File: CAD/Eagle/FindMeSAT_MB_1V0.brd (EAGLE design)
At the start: 99 x 49.2 mm, 127 parts, among them IC1111 LM2831YMF, J291 MCX-J-P-X-RA-SM1, J685 SMA_CON, J701 MOLEX_105017-0001, J801 MICROSIM-8P_SDCARD-8P_MOLEX-1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, J901 JST_S3B-XH-A, Q101 ABS07, Q651 ABM3B-16MHZ-10-R50-1-U, U1001 CFPT-141, U101 ATXMEGA256A3BU-AU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

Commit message: Eagle - minor changes done
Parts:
- moved R701 0.64 mm to (94.2, 32.3)
- moved R721 0.64 mm to (90.3, 22.9)
- moved C701 0.63 mm to (91.3, 32.9)
- moved R724 0.63 mm to (91.3, 29.8)
- moved R725 0.63 mm to (90.8, 29.8)
- moved J701 0.51 mm to (98.6, 27.9)
- moved J801 0.25 mm to (26.8, 8.89)
- moved R141 0.18 mm to (71.0, 4.95)
- moved R142 0.13 mm to (71.0, 3.68)
- renumbered IC1111 to U1111
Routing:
- net +3V3: track 58.0 -> 63.1 mm, vias 15 -> 16
- net GND: track 214.5 -> 216.0 mm
- net +5V: track 130.4 -> 129.0 mm
- net J_VUSB: track 7.64 -> 8.29 mm
- net USB_ID: track 38.7 -> 38.0 mm
- net GPS_1PPS: track 52.3 -> 52.8 mm
- net J_D-: track 9.04 -> 8.53 mm
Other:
- board text added: "+"
- board text added: "Bluetooth-Antenna"
- board text added: "GND"
- board text added: "GPS"
- board text added: "GSM-Antenna"
- board text added: "LCD"
- board text added: "LiPo"
- board text added: "PDI"
- board text added: "USB"
- board text added: "VHF"

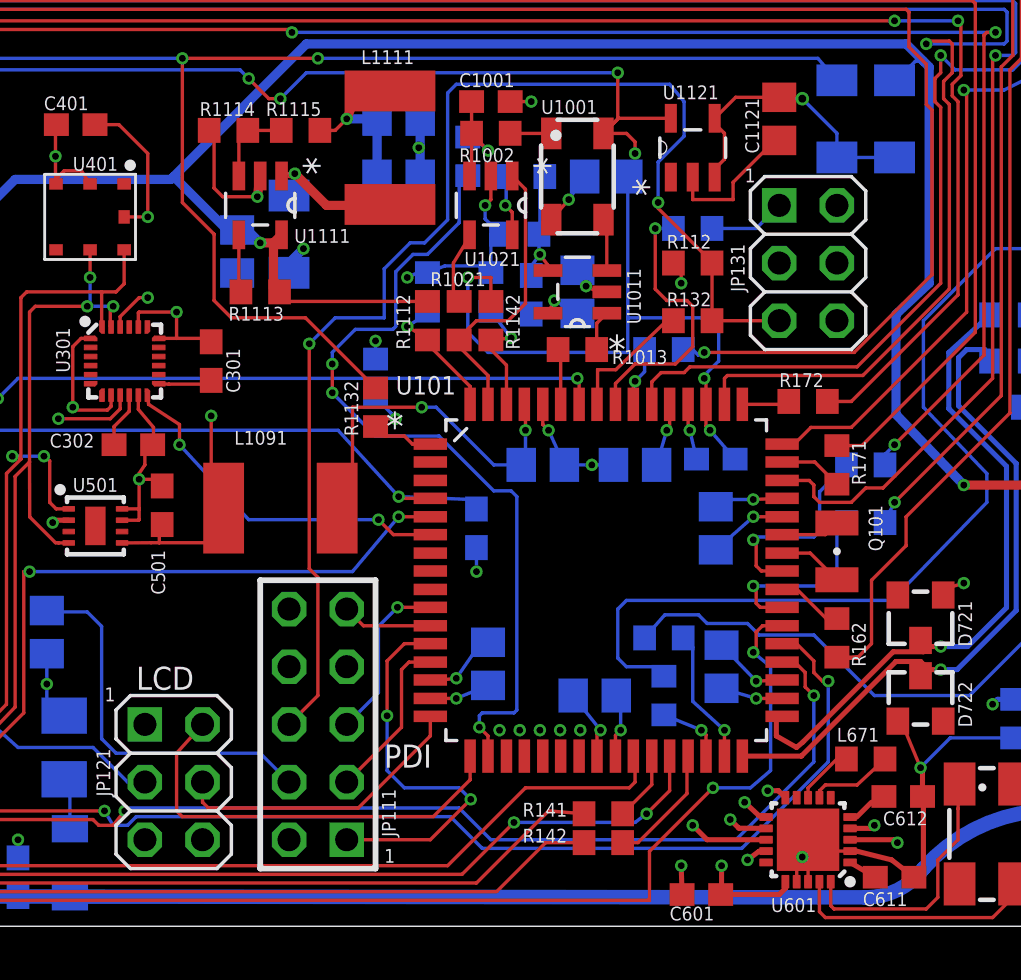
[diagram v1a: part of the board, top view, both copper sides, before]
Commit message: Eagle - values corrected and placed
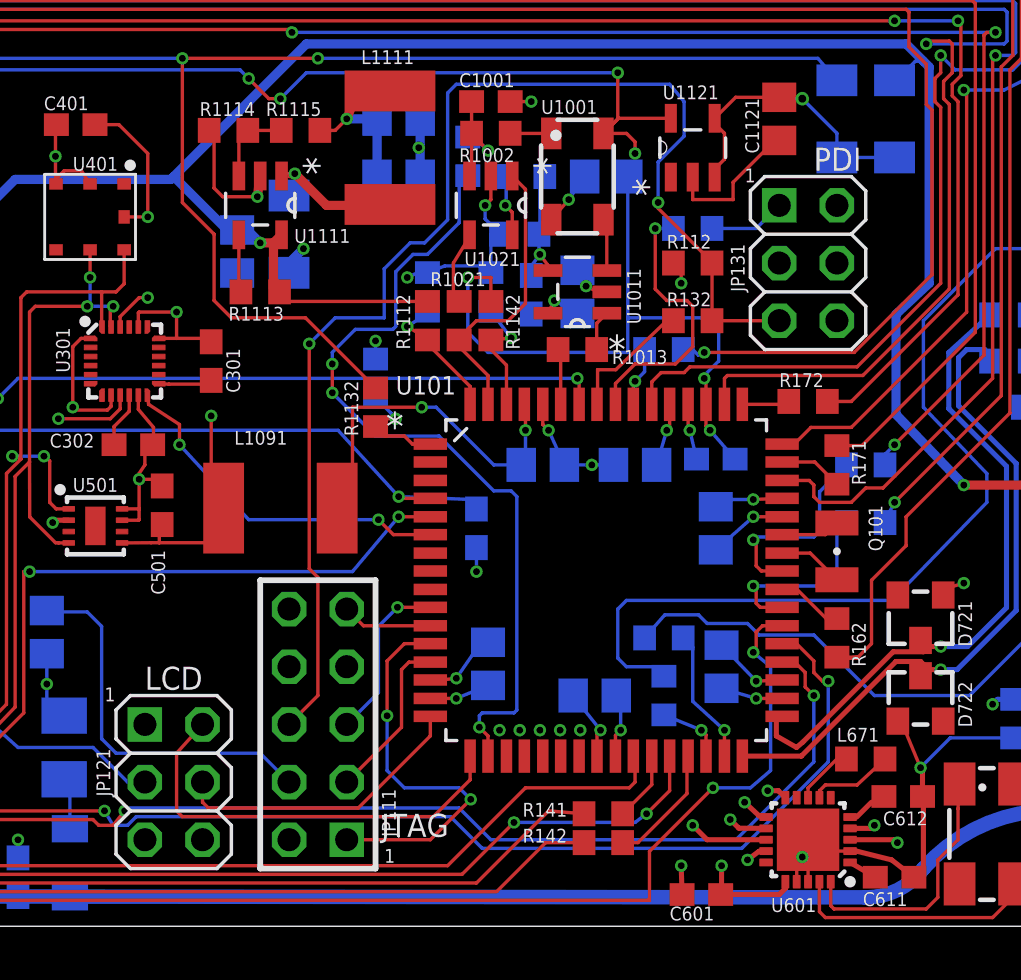
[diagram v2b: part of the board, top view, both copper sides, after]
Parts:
- JP111: value JTAG -> (none)
- JP121: value DISPLAY -> (none)
- JP131: value PDI -> (none)
- U301: value 9DoF IMU -> MPU-9250
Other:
- board text added: "JTAG"

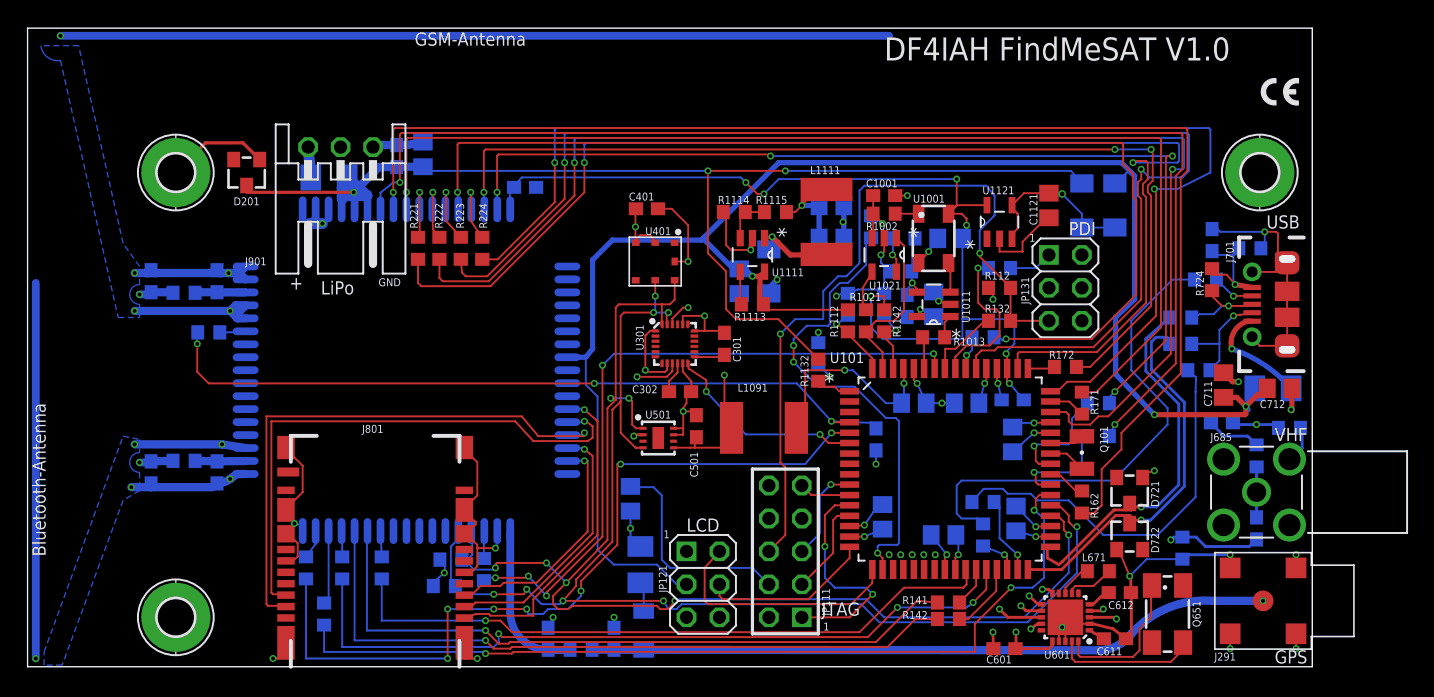
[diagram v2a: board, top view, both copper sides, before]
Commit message: Eagle - some more trimming and library corrections done
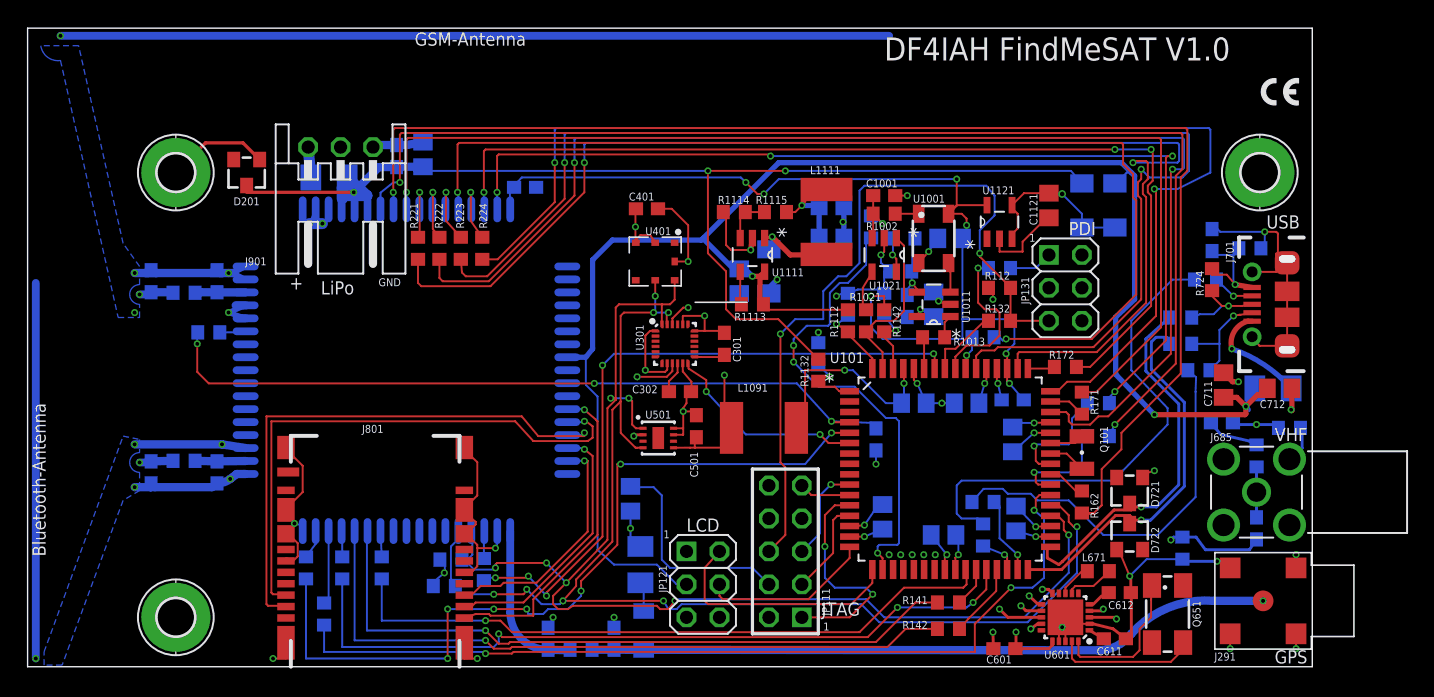
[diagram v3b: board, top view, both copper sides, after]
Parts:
- U301: value MPU-9250 -> 9DoF IMU
- moved R142 0.76 mm to (71.0, 2.92)
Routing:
- net GND: track 216.0 -> 206.7 mm

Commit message: Eagle - design checks and corrections made on board and in libary entries
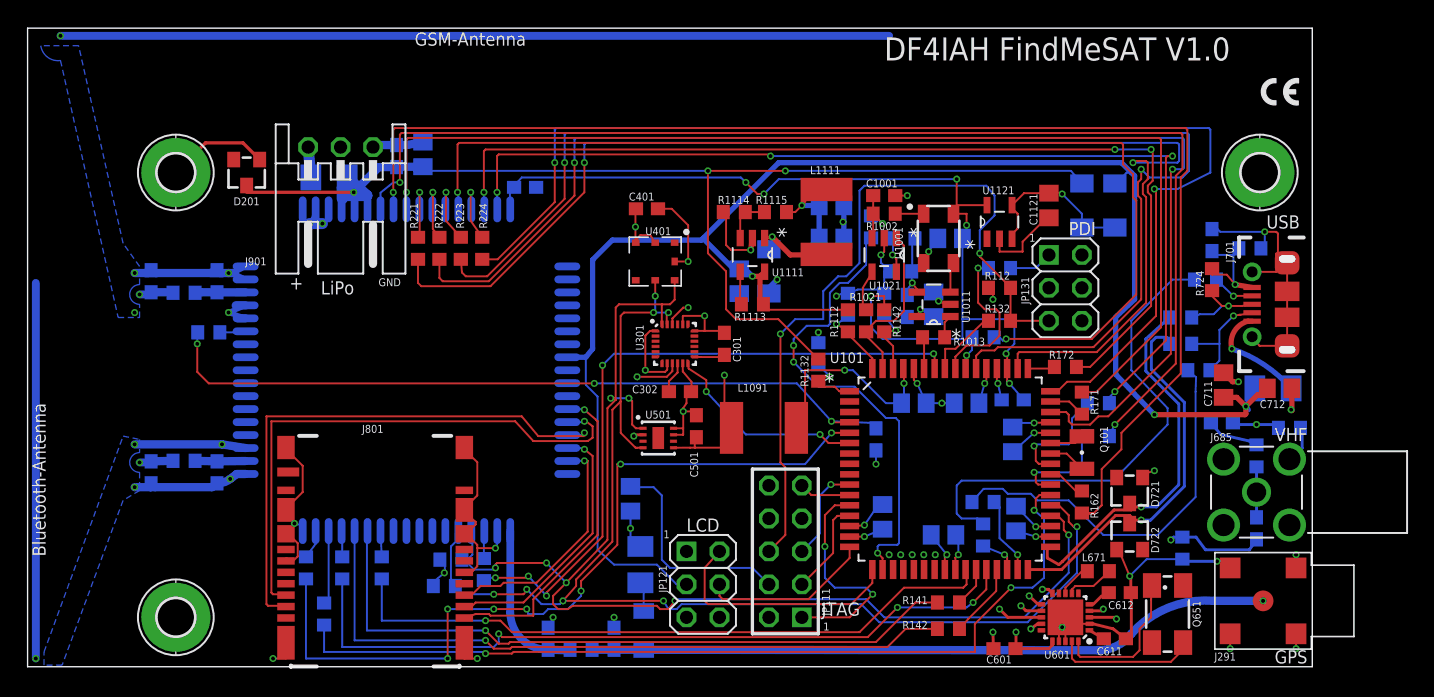
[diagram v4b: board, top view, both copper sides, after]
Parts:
- moved U1001 0.38 mm to (70.2, 33.0), turned to 0 degrees
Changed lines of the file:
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@@
 <layer number="27" name="tValues" color="5" fill="1" visible="no" active="yes"/>
 <layer number="28" name="bValues" color="5" fill="1" visible="no" active="yes"/>
-<layer number="29" name="tStop" color="7" fill="3" visible="no" active="yes"/>
-<layer number="30" name="bStop" color="7" fill="6" visible="no" active="yes"/>
-<layer number="31" name="tCream" color="7" fill="4" visible="no" active="yes"/>
-<layer number="32" name="bCream" color="7" fill="5" visible="no" active="yes"/>
+<layer number="29" name="tStop" color="7" fill="3" visible="yes" active="yes"/>
+<layer number="30" name="bStop" color="7" fill="6" visible="yes" active="yes"/>
+<layer number="31" name="tCream" color="7" fill="4" visible="yes" active="yes"/>
+<layer number="32" name="bCream" color="7" fill="5" visible="yes" active="yes"/>
 <layer number="33" name="tFinish" color="6" fill="3" visible="no" active="yes"/>
 <layer number="34" name="bFinish" color="6" fill="6" visible="no" active="yes"/>
@@
 <layer number="37" name="tTest" color="7" fill="1" visible="no" active="yes"/>
 <layer number="38" name="bTest" color="7" fill="1" visible="no" active="yes"/>
-<layer number="39" name="tKeepout" color="4" fill="11" visible="no" active="yes"/>
-<layer number="40" name="bKeepout" color="1" fill="11" visible="no" active="yes"/>
-<layer number="41" name="tRestrict" color="4" fill="10" visible="no" active="yes"/>
-<layer number="42" name="bRestrict" color="1" fill="10" visible="no" active="yes"/>
-<layer number="43" name="vRestrict" color="2" fill="10" visible="no" active="yes"/>
+<layer number="39" name="tKeepout" color="4" fill="11" visible="yes" active="yes"/>
+<layer number="40" name="bKeepout" color="1" fill="11" visible="yes" active="yes"/>
+<layer number="41" name="tRestrict" color="4" fill="10" visible="yes" active="yes"/>
+<layer number="42" name="bRestrict" color="1" fill="10" visible="yes" active="yes"/>
+<layer number="43" name="vRestrict" color="2" fill="10" visible="yes" active="yes"/>
 <layer number="44" name="Drills" color="7" fill="1" visible="no" active="yes"/>
 <layer number="45" name="Holes" color="7" fill="1" visible="no" active="yes"/>
-<layer number="46" name="Milling" color="3" fill="1" visible="no" active="yes"/>
+<layer number="46" name="Milling" color="3" fill="1" visible="yes" active="yes"/>
 <layer number="47" name="Measures" color="7" fill="1" visible="yes" active="yes"/>
-<layer number="48" name="Document" color="7" fill="1" visible="yes" active="yes"/>
+<layer number="48" name="Document" color="7" fill="1" visible="no" active="yes"/>
 <layer number="49" name="Reference" color="7" fill="1" visible="yes" active="yes"/>
 <layer number="50" name="dxf" color="7" fill="1" visible="no" active="no"/>
@@
 <attribute name="VALUE" x="76.708" y="20.32" size="0.6096" layer="28" rot="MR0"/>
 </element>
-<element name="U1001" library="df4iah_osc" package="CFPT-141" value="CFPT-141" x="69.85" y="33.02" smashed="yes" rot="R270">
-<attribute name="OC_FARNELL" value="1100745" x="69.85" y="33.02" size="0.6096" layer="27" rot="R270" display="off"/>
-<attribute name="OC_NEWARK" value="-" x="69.85" y="33.02" size="0.6096" layer="27" rot="R270" display="off"/>
-<attribute name="MPN" value="LFTVXO022175" x="69.85" y="33.02" size="0.6096" layer="27" rot="R270" display="off"/>
-<attribute name="MF" value="IQD-FREQUENCY-PRODUCTS" x="69.85" y="33.02" size="0.6096" layer="27" rot="R270" display="off"/>
-<attribute name="NAME" x="68.2558" y="35.780103125" size="0.6096" layer="25"/>
-<attribute name="VALUE" x="70.097525" y="31.01766875" size="0.6096" layer="27" rot="R90"/>
+<element name="U1001" library="df4iah_osc" package="CFPT-141" value="CFPT-141" x="70.231" y="33.02" smashed="yes">
+<attribute name="OC_FARNELL" value="1100745" x="70.231" y="33.02" size="0.6096" layer="27" display="off"/>
+<attribute name="OC_NEWARK" value="-" x="70.231" y="33.02" size="0.6096" layer="27" display="off"/>
+<attribute name="MPN" value="LFTVXO022175" x="70.231" y="33.02" size="0.6096" layer="27" display="off"/>
+<attribute name="MF" value="IQD-FREQUENCY-PRODUCTS" x="70.231" y="33.02" size="0.6096" layer="27" display="off"/>
+<attribute name="NAME" x="67.470896875" y="31.4258" size="0.6096" layer="25" rot="R90"/>
+<attribute name="VALUE" x="72.23333125" y="33.267525" size="0.6096" layer="27" rot="R180"/>
 </element>
 <element name="C1002" library="rcl" package="C0805" value="100n" x="71.12" y="33.02" smashed="yes" rot="MR0">
@@
 <wire x1="71.12" y1="27.94" x2="70.231" y2="28.194" width="0.15" layer="1" curve="-31.890792"/>
 <via x="69.469" y="32.004" extent="1-16" drill="0.3" shape="octagon"/>
-<wire x1="68.7" y1="31.12" x2="69.469" y2="32.004" width="0.15" layer="1"/>
+<wire x1="69.081" y1="31.12" x2="69.469" y2="32.004" width="0.15" layer="1"/>
 <wire x1="70.17" y1="33.02" x2="69.469" y2="32.004" width="0.15" layer="16"/>
 <via x="67.818" y="36.322" extent="1-16" drill="0.3" shape="octagon"/>
@@
 <wire x1="37.21" y1="35.26" x2="37.172" y2="36.963" width="0.15" layer="16"/>
 <wire x1="37.172" y1="36.963" x2="37.504" y2="36.957" width="0.15" layer="16"/>
-<wire x1="71" y1="34.92" x2="71.38" y2="35.3" width="0.15" layer="1"/>
+<wire x1="71.381" y1="34.92" x2="71.38" y2="35.3" width="0.15" layer="1"/>
 <wire x1="71.38" y1="35.3" x2="71.6654" y2="35.5854" width="0.15" layer="1"/>
 <wire x1="71.6654" y1="35.5854" x2="73.9648" y2="35.5854" width="0.15" layer="1"/>
@@
 <wire x1="72.07" y1="33.02" x2="72.39" y2="33.34" width="0.15" layer="16"/>
 <wire x1="72.39" y1="33.34" x2="72.39" y2="34.036" width="0.15" layer="16"/>
-<wire x1="71" y1="34.92" x2="72.014" y2="34.92" width="0.15" layer="1"/>
-<wire x1="72.014" y1="34.92" x2="72.39" y2="34.544" width="0.15" layer="1"/>
-<wire x1="72.39" y1="34.544" x2="72.39" y2="34.036" width="0.15" layer="1"/>
+<wire x1="72.39" y1="34.92" x2="72.39" y2="34.036" width="0.15" layer="1"/>
 <via x="65.024" y="28.575" extent="1-16" drill="0.3" shape="octagon"/>
 <wire x1="66.04" y1="27.52" x2="66.04" y2="28.575" width="0.15" layer="1"/>
@@
 <wire x1="75.438" y1="24.13" x2="75.5142" y2="24.0538" width="0.15" layer="1"/>
 <wire x1="75.5142" y1="24.0538" x2="75.5142" y2="22.987" width="0.15" layer="1"/>
+<wire x1="71.381" y1="34.92" x2="72.39" y2="34.92" width="0.15" layer="1"/>
 </signal>
 <signal name="XO_LP">
@@
 <wire x1="71.1454" y1="30.4546" x2="71.12" y2="30.48" width="0.15" layer="1"/>
 <wire x1="71.12" y1="30.48" x2="71.12" y2="31" width="0.15" layer="1"/>
-<wire x1="71.12" y1="31" x2="71" y2="31.12" width="0.15" layer="1"/>
+<wire x1="71.12" y1="31" x2="71.381" y2="31.12" width="0.15" layer="1"/>
 </signal>
 <signal name="TCXO_20MHZ">
@@
 <wire x1="81.28" y1="33.86" x2="81.28" y2="34.925" width="0.15" layer="16"/>
 <wire x1="81.28" y1="34.925" x2="79.756" y2="36.449" width="0.15" layer="16"/>
-<via x="79.756" y="36.449" extent="1-16" drill="0.35" shape="octagon"/>
+<via x="79.756" y="36.449" extent="1-16" drill="0.3" shape="octagon"/>
 <wire x1="79.756" y1="36.449" x2="79.695" y2="36.51" width="0.15" layer="1"/>
 <wire x1="79.695" y1="36.51" x2="78.74" y2="36.51" width="0.15" layer="1"/>
@@
 <contactref element="U1001" pad="1"/>
 <contactref element="R1002" pad="2"/>
-<wire x1="68.7" y1="34.92" x2="66.895" y2="34.92" width="0.15" layer="1"/>
+<wire x1="69.081" y1="34.92" x2="66.895" y2="34.92" width="0.15" layer="1"/>
 <wire x1="66.895" y1="34.92" x2="66.89" y2="34.925" width="0.15" layer="1"/>
 </signal>
